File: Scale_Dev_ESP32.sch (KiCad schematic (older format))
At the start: 71 parts, among them CON1 USB-MINI-B, IC1 MCP73831, J1 BUTTON, J2 Jack-DC, J3 USB_B_Micro, M1 ESP-WROOM-32, P1 LIPO, Q1 IRLML5203, Q2 S8050, Q3 S8050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

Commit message: update pcb footprint
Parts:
- removed CON1: USB-MINI-B, Scale:USB_Micro-B_SMD_NEW_1, symbol Scale_Dev_ESP32-rescue:USB-MINI-B-Hornbill-Devboard-rescue-Hornbill-Devboard-re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
- added CON1: USB_B_Micro, Connectors_USB:USB_Micro-B_Molex-105017-0001, symbol Connector:USB_B_Micro
- CON2: renamed from J3; footprint Connector_USB:USB_Mini-B_Lumberg_2486_01_Horizontal -> Connectors_USB:USB_Micro-B_Molex-105017-0001
- D2, D3, D4: footprint LEDs:LED-0603 -> Diodes_SMD:D_0603
- D5: symbol SMF05C:SMF05C -> Scale_Dev_ESP32-rescue:SMF05C-SMF05C
- J2: footprint (none) -> Connectors:BARREL_JACK
- U1: symbol cp2110:CP2110 -> Scale_Dev_ESP32-rescue:CP2110-cp2110
- U6, U7, U8, U9: footprint Mounting_Holes:MountingHole_2-5mm -> Mounting_Holes:MountingHole_2.5mm
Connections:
- wire segments 256 -> 261
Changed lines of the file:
@@
 F 0 "D3" V 4310 1805 50  0000 C CNN
 F 1 "LED" V 4220 1805 50  0000 C CNN
-F 2 "LEDs:LED-0603" H 4250 1955 50  0001 C CNN
+F 2 "Diodes_SMD:D_0603" H 4250 1955 50  0001 C CNN
 F 3 "" H 4250 1955 50  0000 C CNN
 	1    4250 1955
@@
 F 0 "D2" V 7460 1870 50  0000 C CNN
 F 1 "Yellow" V 7490 1560 50  0000 C CNN
-F 2 "LEDs:LED-0603" H 7450 1760 50  0001 C CNN
+F 2 "Diodes_SMD:D_0603" H 7450 1760 50  0001 C CNN
 F 3 "" H 7450 1760 50  0000 C CNN
 	1    7450 1760
@@
 F 0 "D4" H 2360 7310 50  0000 C CNN
 F 1 "Blue" H 2360 7390 50  0000 C CNN
-F 2 "LEDs:LED-0603" H 2350 7180 50  0001 C CNN
+F 2 "Diodes_SMD:D_0603" H 2350 7180 50  0001 C CNN
 F 3 "" H 2350 7180 50  0000 C CNN
 	1    2350 7180
@@
 F 0 "U6" H 6210 6880 40  0000 C CNN
 F 1 "MountingHole" H 6210 6930 40  0000 C CNN
-F 2 "Mounting_Holes:MountingHole_2-5mm" H 6210 7030 40  0001 C CNN
+F 2 "Mounting_Holes:MountingHole_2.5mm" H 6210 7030 40  0001 C CNN
 F 3 "" H 6210 7030 40  0000 C CNN
 	1    6210 7030
@@
 F 0 "U8" H 6700 6880 40  0000 C CNN
 F 1 "MountingHole" H 6700 6930 40  0000 C CNN
-F 2 "Mounting_Holes:MountingHole_2-5mm" H 6700 7030 40  0001 C CNN
+F 2 "Mounting_Holes:MountingHole_2.5mm" H 6700 7030 40  0001 C CNN
 F 3 "" H 6700 7030 40  0000 C CNN
 	1    6700 7030
@@
 F 0 "U7" H 6210 7240 40  0000 C CNN
 F 1 "MountingHole" H 6210 7290 40  0000 C CNN
-F 2 "Mounting_Holes:MountingHole_2-5mm" H 6210 7390 40  0001 C CNN
+F 2 "Mounting_Holes:MountingHole_2.5mm" H 6210 7390 40  0001 C CNN
 F 3 "" H 6210 7390 40  0000 C CNN
 	1    6210 7390
@@
 F 0 "U9" H 6710 7240 40  0000 C CNN
 F 1 "MountingHole" H 6710 7290 40  0000 C CNN
-F 2 "Mounting_Holes:MountingHole_2-5mm" H 6710 7390 40  0001 C CNN
+F 2 "Mounting_Holes:MountingHole_2.5mm" H 6710 7390 40  0001 C CNN
 F 3 "" H 6710 7390 40  0000 C CNN
 	1    6710 7390
@@
 Text Label 10000 5350 0    60   ~ 0
 RTS
-$Comp
-L Scale_Dev_ESP32-rescue:USB-MINI-B-Hornbill-Devboard-rescue-Hornbill-Devboard-rescue CON1
-U 1 1 58EC0EA8
-P 6600 5650
-F 0 "CON1" H 6300 6000 50  0000 C CNN
-F 1 "USB-MINI-B" H 6450 5300 50  0000 C CNN
-F 2 "Scale:USB_Micro-B_SMD_NEW_1" H 6600 5550 50  0001 C CNN
-F 3 "" H 6600 5550 50  0000 C CNN
-	1    6600 5650
-	-1   0    0    -1
-$EndComp
 $Comp
 L Scale_Dev_ESP32-rescue:C-Hornbill-Devboard-rescue-Hornbill-Devboard-rescue C3
@@
 	10000 5650 10450 5650
 Wire Wire Line
-	7650 5550 7100 5550
-Wire Wire Line
-	7100 5650 7650 5650
-Wire Wire Line
 	7100 5850 7400 5850
 Wire Wire Line
@@
 	7650 5450 7650 4550
 Connection ~ 7650 4550
-Wire Wire Line
-	7200 5450 7100 5450
 Wire Wire Line
 	7500 5450 7650 5450
@@
 F 0 "J2" H 8605 1175 50  0000 C CNN
 F 1 "Jack-DC" H 8605 1084 50  0000 C CNN
-F 2 "" H 8600 810 50  0001 C CNN
+F 2 "Connectors:BARREL_JACK" H 8600 810 50  0001 C CNN
 F 3 "~" H 8600 810 50  0001 C CNN
 	1    8550 850
@@
 	8850 650  8850 750
 $Comp
-L cp2110:CP2110 U1
+L Scale_Dev_ESP32-rescue:CP2110-cp2110 U1
 U 1 1 5BC656A4
 P 13450 1800
@@
 $EndComp
 $Comp
-L Connector:USB_B_Micro J3
+L Connector:USB_B_Micro CON2
 U 1 1 5BCFAE51
 P 10350 950
-F 0 "J3" H 10405 1417 50  0000 C CNN
+F 0 "CON2" H 10405 1417 50  0000 C CNN
 F 1 "USB_B_Micro" H 10405 1326 50  0000 C CNN
-F 2 "Connector_USB:USB_Mini-B_Lumberg_2486_01_Horizontal" H 10500 900 50  0001 C CNN
+F 2 "Connectors_USB:USB_Micro-B_Molex-105017-0001" H 10500 900 50  0001 C CNN
 F 3 "~" H 10500 900 50  0001 C CNN
 	1    10350 950
@@
 	10250 1400 10250 1450
 $Comp
-L SMF05C:SMF05C D5
+L Scale_Dev_ESP32-rescue:SMF05C-SMF05C D5
 U 1 1 5BE083F1
 P 11100 1900
@@
 Wire Wire Line
 	8850 1050 8850 1100
+$Comp
+L Connector:USB_B_Micro CON1
+U 1 1 5BC7A30E
+P 6575 5650
+F 0 "CON1" H 6630 6117 50  0000 C CNN
+F 1 "USB_B_Micro" H 6630 6026 50  0000 C CNN
+F 2 "Connectors_USB:USB_Micro-B_Molex-105017-0001" H 6725 5600 50  0001 C CNN
+F 3 "~" H 6725 5600 50  0001 C CNN
+	1    6575 5650
+	1    0    0    -1
+$EndComp
+Wire Wire Line
+	6875 5450 7200 5450
+Wire Wire Line
+	6875 5650 7650 5650
+Wire Wire Line
+	6875 5750 6950 5750
+Wire Wire Line
+	6950 5750 6950 5550
+Wire Wire Line
+	6950 5550 7650 5550
+Wire Wire Line
+	6575 6050 7100 6050
+Wire Wire Line
+	7100 6050 7100 5850
+Wire Wire Line
+	6475 6050 6575 6050
+Connection ~ 6575 6050
 $EndSCHEMATC

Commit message: place pcb items
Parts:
- added TP1, TP2, TP3, TP4: TestPoint, TestPoint:TestPoint_Pad_D4.0mm, symbol Connector:TestPoint
- C1, C6: footprint Capacitor_SMD:C_0805_2012Metric_Pad1.15x1.40mm_HandSolder -> Capacitor_SMD:CP_Elec_4x3
- C15: value CP -> 10uF
- C17, C18: footprint Capacitor_SMD:CP_Elec_4x3 -> Capacitor_SMD:C_0805_2012Metric_Pad1.15x1.40mm_HandSolder
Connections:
- net IO12 is gone; now on net BUT0: M1.14 (IO12)
- net IO27 is gone; now on net BUT1: M1.12 (IO27)
- net BUT0: now also TP1.1; no longer M1.23 (IO15)
- net BUT1: now also TP2.1; no longer M1.24 (IO2)
- net BUT2: now also TP3.1
- net BUT3: now also M1.24 (IO2), TP4.1; no longer M1.16 (IO13)
- net IO13: now also M1.16 (IO13)
- net IO15: now also M1.23 (IO15)
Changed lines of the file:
@@
 IO26
 Text Label 2530 5910 2    60   ~ 0
-IO27
+BUT1
 Text Label 2530 6010 2    60   ~ 0
 IO14
 Text Label 2530 6110 2    60   ~ 0
-IO12
+BUT0
 Text Label 3450 6619 3    60   ~ 0
-BUT3
+IO13
 Text Label 3550 6620 3    60   ~ 0
 SD2
@@
 SD1
 Text Label 4150 6620 3    60   ~ 0
-BUT0
+IO15
 Text Label 4250 6620 3    60   ~ 0
-BUT1
+BUT3
 Text Label 5160 4910 0    60   ~ 0
 IO23
@@
 F 0 "C1" H 5375 1660 50  0000 L CNN
 F 1 "4.7uF" H 5375 1460 50  0000 L CNN
-F 2 "Capacitor_SMD:C_0805_2012Metric_Pad1.15x1.40mm_HandSolder" H 5388 1410 50  0001 C CNN
+F 2 "Capacitor_SMD:CP_Elec_4x3" H 5388 1410 50  0001 C CNN
 F 3 "" H 5350 1560 50  0000 C CNN
 	1    5350 1560
@@
 F 0 "C6" H 7965 1610 50  0000 L CNN
 F 1 "4.7uF" H 7965 1410 50  0000 L CNN
-F 2 "Capacitor_SMD:C_0805_2012Metric_Pad1.15x1.40mm_HandSolder" H 7978 1360 50  0001 C CNN
+F 2 "Capacitor_SMD:CP_Elec_4x3" H 7978 1360 50  0001 C CNN
 F 3 "" H 7940 1510 50  0000 C CNN
 	1    7940 1510
@@
 F 0 "C18" H 12468 1896 50  0000 L CNN
 F 1 "1uF" H 12468 1805 50  0000 L CNN
-F 2 "Capacitor_SMD:CP_Elec_4x3" H 12388 1700 50  0001 C CNN
+F 2 "Capacitor_SMD:C_0805_2012Metric_Pad1.15x1.40mm_HandSolder" H 12388 1700 50  0001 C CNN
 F 3 "~" H 12350 1850 50  0001 C CNN
 	1    12350 1850
@@
 F 0 "C17" H 12265 1896 50  0000 L CNN
 F 1 "0.1uF" H 12265 1805 50  0000 L CNN
-F 2 "Capacitor_SMD:CP_Elec_4x3" H 12188 1700 50  0001 C CNN
+F 2 "Capacitor_SMD:C_0805_2012Metric_Pad1.15x1.40mm_HandSolder" H 12188 1700 50  0001 C CNN
 F 3 "~" H 12150 1850 50  0001 C CNN
 	1    12150 1850
@@
 P 9100 900
 F 0 "C15" H 9218 946 50  0000 L CNN
-F 1 "CP" H 9218 855 50  0000 L CNN
+F 1 "10uF" H 9218 855 50  0000 L CNN
 F 2 "Capacitor_SMD:CP_Elec_4x3" H 9138 750 50  0001 C CNN
 F 3 "~" H 9100 900 50  0001 C CNN
@@
 	6475 6050 6575 6050
 Connection ~ 6575 6050
+$Comp
+L Connector:TestPoint TP1
+U 1 1 5BC8B2F5
+P 2750 9200
+F 0 "TP1" H 2808 9320 50  0000 L CNN
+F 1 "TestPoint" H 2808 9229 50  0000 L CNN
+F 2 "TestPoint:TestPoint_Pad_D4.0mm" H 2950 9200 50  0001 C CNN
+F 3 "~" H 2950 9200 50  0001 C CNN
+	1    2750 9200
+	1    0    0    -1
+$EndComp
+$Comp
+L Connector:TestPoint TP2
+U 1 1 5BC8B497
+P 2900 9300
+F 0 "TP2" H 2958 9420 50  0000 L CNN
+F 1 "TestPoint" H 2958 9329 50  0000 L CNN
+F 2 "TestPoint:TestPoint_Pad_D4.0mm" H 3100 9300 50  0001 C CNN
+F 3 "~" H 3100 9300 50  0001 C CNN
+	1    2900 9300
+	1    0    0    -1
+$EndComp
+$Comp
+L Connector:TestPoint TP3
+U 1 1 5BC8B5B2
+P 3000 9400
+F 0 "TP3" H 3058 9520 50  0000 L CNN
+F 1 "TestPoint" H 3058 9429 50  0000 L CNN
+F 2 "TestPoint:TestPoint_Pad_D4.0mm" H 3200 9400 50  0001 C CNN
+F 3 "~" H 3200 9400 50  0001 C CNN
+	1    3000 9400
+	1    0    0    -1
+$EndComp
+$Comp
+L Connector:TestPoint TP4
+U 1 1 5BC8B6E0
+P 3250 9500
+F 0 "TP4" H 3308 9620 50  0000 L CNN
+F 1 "TestPoint" H 3308 9529 50  0000 L CNN
+F 2 "TestPoint:TestPoint_Pad_D4.0mm" H 3450 9500 50  0001 C CNN
+F 3 "~" H 3450 9500 50  0001 C CNN
+	1    3250 9500
+	1    0    0    -1
+$EndComp
+Wire Wire Line
+	2750 9200 2150 9200
+Wire Wire Line
+	2900 9300 2250 9300
+Wire Wire Line
+	3000 9400 2350 9400
+Wire Wire Line
+	3250 9500 2450 9500
 $EndSCHEMATC

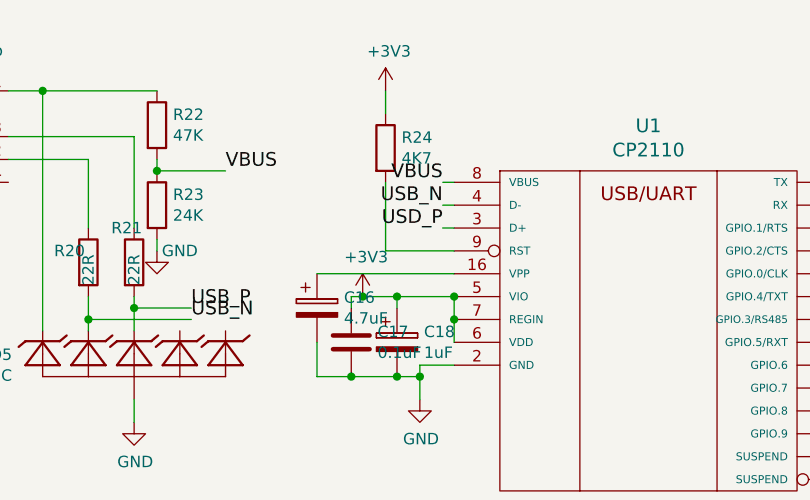
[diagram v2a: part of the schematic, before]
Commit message: update pcb route
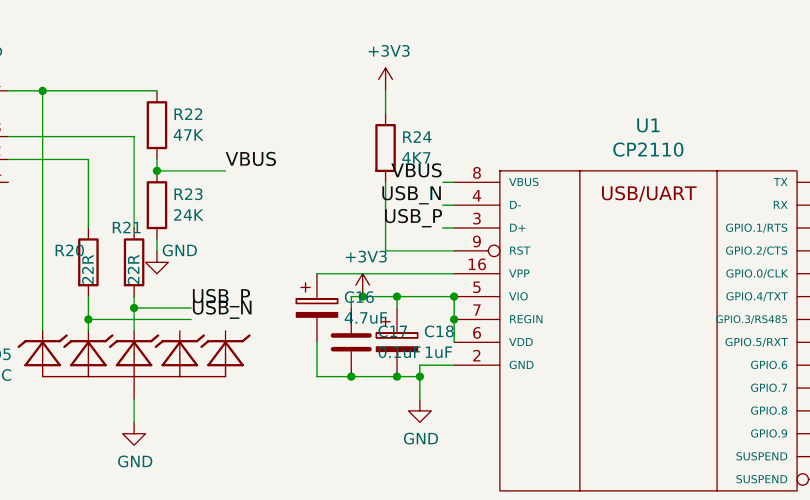
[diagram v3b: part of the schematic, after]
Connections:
- net USD_P is gone; now on net USB_P: U1.3 (D+)
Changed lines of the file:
@@
 	12600 1350 12550 1350
 Text Label 12550 1350 2    60   ~ 0
-USD_P
+USB_P
 Text Label 12550 1250 2    60   ~ 0
 USB_N
